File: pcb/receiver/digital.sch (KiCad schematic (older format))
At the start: 0 parts

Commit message: Add all components TODO footprint/source everything
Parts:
- added C301: 1 uF, symbol Device:C_Small
- added C302, C303, C304, C305, C306, C307, C308, C309, C312, C316, C317, C318, C320, C321: 100 nF, symbol Device:C_Small
- added C310: 4.7 uF, symbol Device:C_Small
- added C311, C313: C_Small, symbol Device:C_Small
- added C314, C315, C319: 10 uF, symbol Device:C_Small
- added C322, C323: 22 pF, symbol Device:C_Small
- added D301: D_Schottky, symbol Device:D_Schottky
- added D302, D303: 2SS100L-W, symbol Device:D_Schottky_Small
- added D304, D305, D306: TPD1E04U04DPYR, symbol Device:D_Small
- added J301, J303: Conn_01x03, symbol Connector_Generic:Conn_01x03
- added J302: Conn_01x04, symbol Connector_Generic:Conn_01x04
- added J304: USB_B_Micro, symbol Connector:USB_B_Micro
- added R301, R302, R305: 0 DNP, symbol Device:R_Small
- added R303, R304: 0, symbol Device:R_Small
- added R306, R307: 1M, symbol Device:R_Small
- added R308, R309: R_Small, symbol Device:R_Small
- added R310, R317: 10k, symbol Device:R_Small
- added R311: 100k DNP, symbol Device:R_Small
- added R312, R313: 100k, symbol Device:R_Small
- added R314, R315, R316: 330, symbol Device:R_Small
- added R318: 10k DNP, symbol Device:R_Small
- added U301: ATTINY412-SSNR, symbol receiver:ATTINY412-SSNR
- added U302: STM32F070F6P6, symbol receiver:STM32F070F6P6
- added U303: MAX11666AUB+T, symbol receiver:MAX11666AUB+T
- added U304: L78L33ABUTR, symbol receiver:L78L33ABUTR
- added Y301: ABM3B-8.000MHZ-10-1UT, symbol Device:Crystal_GND24
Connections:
- new net: R317.2, R318.1, U302.1 (BOOT0/WKUP2/RTC_TAMP1/RTC_TS/RTC_OUT)
- new net: C322.1, U302.2 (PF0/OSC_IN), Y301.1
- new net: C323.1, U302.3 (PF1/OSC_OUT), Y301.3
- new net: R310.2, U303.2 (AIN2)
- new net: R312.1, U303.7 (CHSEL)
- new net: C311.2, R306.2, R307.1, R308.1
- new net: J303.2 (Pin_2), R316.2
- new net: J301.2 (Pin_2), R314.2
- new net: J301.3 (Pin_3), R315.2
- new net +3V3: C301.1, C302.1, C305.1, C306.1, C307.1, C308.1, C309.1, C310.1, C318.1, C319.1, C321.1, D301.2 (A), R301.2, R309.1, R313.2, R318.2, U302.16 (VDD), U302.5 (VDDA), U303.8 (DVDD), U304.1 (VOUT)
- new net +3V3A: C312.1, C314.1, C315.1, C316.1, C317.1, D302.1 (K), R306.1, R309.2, U303.4 (REF), U303.5 (VDD)
- new net +3V3_ATTINY: C304.1, D301.1 (K), J303.3 (Pin_3), R301.1, U301.1 (VDD)
- new net +5V_USB: C320.1, D304.1 (K), J304.1 (VBUS), U304.3 (VIN)
- new net ADC_AIN: C311.1
- new net ADC_MISO: U302.12 (PA6/SPI1_MISO/TIM3_CH1/TIM1_BKIN/TIM16_CH1/EVENTOUT/USART3_CTS/ADC_IN6), U303.9 (DOUT)
- new net ADC_MOSI: R311.1, U302.13 (PA7/SPI1_MOSI/TIM3_CH2/TIM14_CH1/TIM1_CH1N/TIM17_CH1/EVENTOUT/ADC_IN7)
- new net ADC_NSS: R313.1, U302.10 (PA4/SPI1_NSS/TIM14_CH1/USART2_CK/USB_NOE/ADC_IN4), U303.6 (nCS)
- new net ADC_SCK: U302.11 (PA5/SPI1_SCK/ADC_IN5), U303.10 (SCLK)
- new net AIN1: C313.1, D302.2 (A), D303.1 (K), R308.2, U303.1 (AIN1)
- new net ANALOG_EN: U302.14 (PB1/TIM3_CH4/USART3_RTS/TIM14_CH1/TIM1_CH3N/ADC_IN9)
- new net ATTINY_RXD: R304.2, R305.2, U301.5 (PA2)
- new net ATTINY_TXD: R302.2, R303.2, U301.4 (PA1)
- new net DEBUG_RX: R315.1, U302.7 (PA1/USART2_RTS/TIM15_CH1N/USART4_RX/EVENTOUT/ADC_IN1)
- new net DEBUG_TX: R314.1, U302.6 (PA0/USART2_CTS/USART4_TX/RTC__TAMP2/WKUP1/ADC_IN0)
- new net GAIN_ADC: U301.3 (PA7)
- new net GAIN_PDM: U301.2 (PA6)
- new net GAIN_SEL: U301.7 (PA3/EXTCLK)
- new net GND: C301.2, C302.2, C303.2, C304.2, C305.2, C306.2, C307.2, C308.2, C309.2, C310.2, C312.2, C313.2, C314.2, C315.2, C316.2, C317.2, C318.2, C319.2, C320.2, C321.2, C322.2, C323.2, D303.2 (A), D304.2 (A), D305.2 (A), D306.2 (A), J301.1 (Pin_1), J302.1 (Pin_1), J303.1 (Pin_1), J304.5 (GND), J304.6 (Shield), R307.2, R310.1, R311.2, R312.2, R317.1, U301.8 (GND), U302.15 (VSS), U303.11 (GPAD), U303.3 (AGND), Y301.2, Y301.4
- new net STM32_NRST: C303.1, J302.2 (Pin_2), U302.4 (NRST)
- new net STM32_RXD: R303.1, R305.1, U302.9 (PA3/USART2_RX/TIM15_CH2/ADC_IN3)
- new net STM32_SWCLK: J302.3 (Pin_3), U302.20 (PA14/USART2_TX/SWCLK)
- new net STM32_SWDIO: J302.4 (Pin_4), U302.19 (PA13/IR_OUT/SWDIO/USB_NOE)
- new net STM32_TXD: R302.1, R304.1, U302.8 (PA2/USART2_TX/TIM15_CH1/ADC_IN2/WKUP4)
- new net UPDI: R316.1, U301.6 (PA0/nRESET/UPDI)
- new net USB_DM: D306.1 (K), J304.2 (D-), U302.17 (PA9/USART1_TX/TIM1_CH2/TIM15_BKIN/I2C1_SCL/USART1_CTS/TIM1_CH4/EVENTOUT/USB_DM)
- new net USB_DP: D305.1 (K), J304.3 (D+), U302.18 (PA10/USART1_RX/TIM1_CH3/TIM17_BKIN/I2C1_SDA/USART1_RTS/TIM1_ETR/EVENTOUT/USB_DP)
- no-connect marks 0 -> 1
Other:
- note added: "+ 6 mA quiescent"
- note added: "1.7 mA"
- note added: "11 mA quiescent, ignoring charging gain input capacitors"
- note added: "<10 mA"

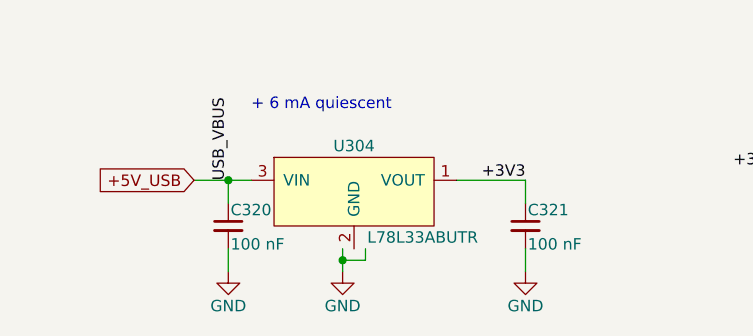
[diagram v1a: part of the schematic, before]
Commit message: Most parts footprinted; TODO analog voltage reference, photodiodes, passives
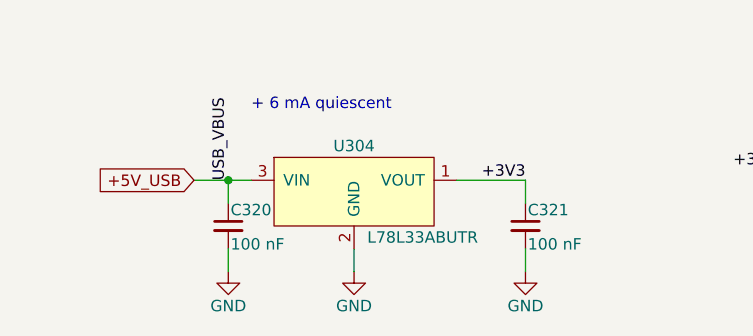
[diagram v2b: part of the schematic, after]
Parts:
- U301: footprint (none) -> receiver-footprints:Atmel-SOIC150-8
- U302: footprint (none) -> receiver-footprints:ST-TSSOP20
- U303: footprint (none) -> receiver-footprints:Maxim-U10E+3
- U304: footprint (none) -> TO_SOT_Packages_SMD:SOT-89-3_Handsoldering
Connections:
- net GND: now also U304.2 (GND)
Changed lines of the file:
@@
 F 0 "U302" H 5550 1200 50  0000 C CNN
 F 1 "STM32F070F6P6" H 5550 -100 50  0000 C CNN
-F 2 "" H 5550 1100 50  0001 C CNN
+F 2 "receiver-footprints:ST-TSSOP20" H 5550 1100 50  0001 C CNN
 F 3 "" H 5550 1100 50  0001 C CNN
 	1    5550 1100
@@
 F 0 "U301" H 5550 5550 50  0000 C CNN
 F 1 "ATTINY412-SSNR" H 5550 4950 50  0000 C CNN
-F 2 "" H 5550 5550 50  0001 C CNN
+F 2 "receiver-footprints:Atmel-SOIC150-8" H 5550 5550 50  0001 C CNN
 F 3 "" H 5550 5550 50  0001 C CNN
 	1    5550 5550
@@
 F 0 "U303" H 6900 3150 50  0000 C CNN
 F 1 "MAX11666AUB+T" H 6900 2250 50  0000 C CNN
-F 2 "" H 6900 3150 50  0001 C CNN
+F 2 "receiver-footprints:Maxim-U10E+3" H 6900 3150 50  0001 C CNN
 F 3 "" H 6900 3150 50  0001 C CNN
 	1    6900 3150
@@
 F 0 "U304" H 2100 5600 50  0000 C CNN
 F 1 "L78L33ABUTR" H 2400 5200 50  0000 C CNN
-F 2 "" H 2100 5600 50  0001 C CNN
+F 2 "TO_SOT_Packages_SMD:SOT-89-3_Handsoldering" H 2100 5600 50  0001 C CNN
 F 3 "" H 2100 5600 50  0001 C CNN
 	1    2100 5600
@@
 L power:GND #PWR0158
 U 1 1 5C3D87E6
-P 2050 6150
-F 0 "#PWR0158" H 2050 5900 50  0001 C CNN
-F 1 "GND" H 2050 6000 50  0000 C CNN
-F 2 "" H 2050 6150 50  0001 C CNN
-F 3 "" H 2050 6150 50  0001 C CNN
-	1    2050 6150
-	1    0    0    -1
-$EndComp
-Wire Wire Line
-	2050 6050 2050 6100
+P 2100 6150
+F 0 "#PWR0158" H 2100 5900 50  0001 C CNN
+F 1 "GND" H 2100 6000 50  0000 C CNN
+F 2 "" H 2100 6150 50  0001 C CNN
+F 3 "" H 2100 6150 50  0001 C CNN
+	1    2100 6150
+	1    0    0    -1
+$EndComp
 Wire Wire Line
 	2850 5750 2550 5750
@@
 Wire Wire Line
 	1550 5750 1650 5750
-Wire Wire Line
-	2150 6050 2150 6100
-Wire Wire Line
-	2150 6100 2050 6100
-Connection ~ 2050 6100
-Wire Wire Line
-	2050 6100 2050 6150
 $Comp
 L Device:C_Small C321
@@
 Wire Wire Line
 	2000 700  2250 700
+Wire Wire Line
+	2100 6050 2100 6150
 $EndSCHEMATC

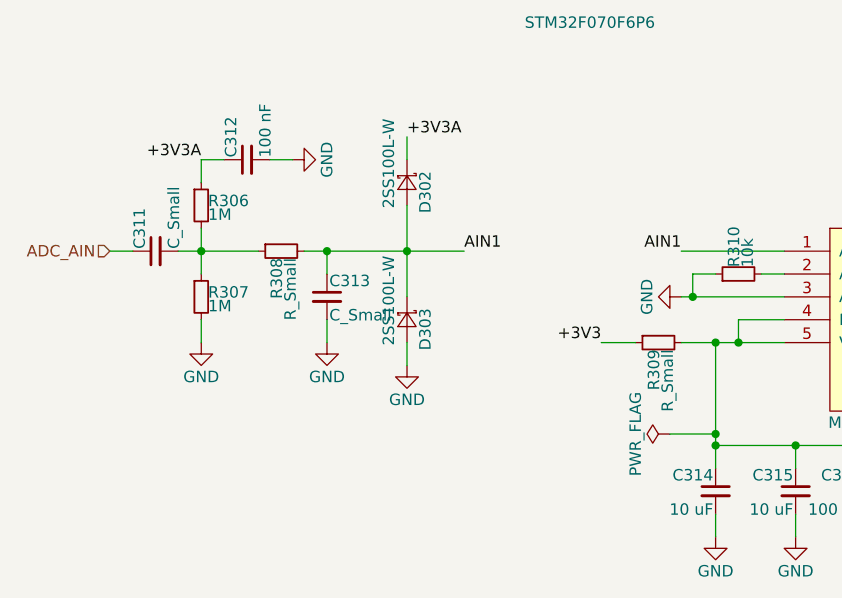
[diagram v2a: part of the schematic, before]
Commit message: Source most passives; save before autofill
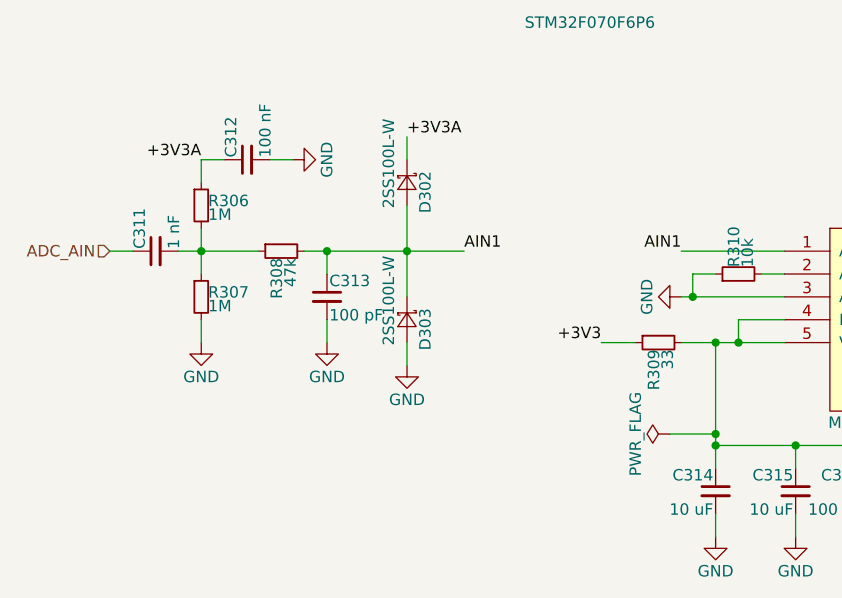
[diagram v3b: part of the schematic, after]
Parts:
- C311: value C_Small -> 1 nF
- C313: value C_Small -> 100 pF; footprint (none) -> Capacitors_SMD:C_0402; Mouser (none) -> 963-UMK105CH101JVHF
- C322: footprint (none) -> Capacitors_SMD:C_0402; Mouser (none) -> 710-885012005009
- R308: value R_Small -> 47k
- R309: value R_Small -> 33
- U301: Mouser (none) -> 556-ATTINY412-SSNR
- U302: Mouser (none) -> 511-STM32F070F6P6
- U303: Mouser (none) -> 700-MAX11666AUB+T
- U304: Mouser (none) -> 511-L78L33ABU-TR
- Y301: footprint (none) -> Crystals:Crystal_SMD_Abracon_ABM3C-4pin_5.0x3.2mm; Mouser (none) -> 815-ABM3B-8.0-10-1UT
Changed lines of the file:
@@
 F 2 "receiver-footprints:ST-TSSOP20" H 5550 1100 50  0001 C CNN
 F 3 "" H 5550 1100 50  0001 C CNN
+F 4 "511-STM32F070F6P6" H 5550 1100 50  0001 C CNN "Mouser"
 	1    5550 1100
 	1    0    0    -1
@@
 F 2 "receiver-footprints:Atmel-SOIC150-8" H 5550 5550 50  0001 C CNN
 F 3 "" H 5550 5550 50  0001 C CNN
+F 4 "556-ATTINY412-SSNR" H 5550 5550 50  0001 C CNN "Mouser"
 	1    5550 5550
 	1    0    0    -1
@@
 F 2 "receiver-footprints:Maxim-U10E+3" H 6900 3150 50  0001 C CNN
 F 3 "" H 6900 3150 50  0001 C CNN
+F 4 "700-MAX11666AUB+T" H 6900 3150 50  0001 C CNN "Mouser"
 	1    6900 3150
 	1    0    0    -1
@@
 P 5850 3700
 F 0 "R309" H 5880 3720 50  0000 L CNN
-F 1 "R_Small" H 5880 3660 50  0000 L CNN
+F 1 "33" H 5880 3660 50  0000 L CNN
 F 2 "" H 5850 3700 50  0001 C CNN
 F 3 "~" H 5850 3700 50  0001 C CNN
@@
 P 3650 3300
 F 0 "C311" H 3660 3370 50  0000 L CNN
-F 1 "C_Small" H 3660 3220 50  0000 L CNN
+F 1 "1 nF" H 3660 3220 50  0000 L CNN
 F 2 "" H 3650 3300 50  0001 C CNN
 F 3 "~" H 3650 3300 50  0001 C CNN
@@
 P 4200 3300
 F 0 "R308" H 4230 3320 50  0000 L CNN
-F 1 "R_Small" H 4230 3260 50  0000 L CNN
+F 1 "47k" H 4230 3260 50  0000 L CNN
 F 2 "" H 4200 3300 50  0001 C CNN
 F 3 "~" H 4200 3300 50  0001 C CNN
@@
 P 4400 3500
 F 0 "C313" H 4410 3570 50  0000 L CNN
-F 1 "C_Small" H 4410 3420 50  0000 L CNN
-F 2 "" H 4400 3500 50  0001 C CNN
+F 1 "100 pF" H 4410 3420 50  0000 L CNN
+F 2 "Capacitors_SMD:C_0402" H 4400 3500 50  0001 C CNN
 F 3 "~" H 4400 3500 50  0001 C CNN
+F 4 "963-UMK105CH101JVHF" H 4400 3500 50  0001 C CNN "Mouser"
 	1    4400 3500
 	1    0    0    -1
@@
 F 2 "TO_SOT_Packages_SMD:SOT-89-3_Handsoldering" H 2100 5600 50  0001 C CNN
 F 3 "" H 2100 5600 50  0001 C CNN
+F 4 "511-L78L33ABU-TR" H 2100 5600 50  0001 C CNN "Mouser"
 	1    2100 5600
 	1    0    0    -1
@@
 F 0 "Y301" H 1275 1300 50  0000 L CNN
 F 1 "ABM3B-8.000MHZ-10-1UT" H 1275 1225 50  0000 L CNN
-F 2 "" H 1150 1100 50  0001 C CNN
+F 2 "Crystals:Crystal_SMD_Abracon_ABM3C-4pin_5.0x3.2mm" H 1150 1100 50  0001 C CNN
 F 3 "~" H 1150 1100 50  0001 C CNN
+F 4 "815-ABM3B-8.0-10-1UT" H 1150 1100 50  0001 C CNN "Mouser"
 	1    1150 1100
 	1    0    0    -1
@@
 F 0 "C322" H 910 1370 50  0000 L CNN
 F 1 "22 pF" H 910 1220 50  0000 L CNN
-F 2 "" H 900 1300 50  0001 C CNN
+F 2 "Capacitors_SMD:C_0402" H 900 1300 50  0001 C CNN
 F 3 "~" H 900 1300 50  0001 C CNN
+F 4 "710-885012005009" H 900 1300 50  0001 C CNN "Mouser"
 	1    900  1300
 	-1   0    0    -1
